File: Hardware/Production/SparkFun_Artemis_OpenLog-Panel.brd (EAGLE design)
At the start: 106.2 x 95.2 mm, 714 parts, among them J11 QWIIC_RIGHT_ANGLE, J14 CORTEX_JTAG, J16 CORTEX_JTAG, J17 MICRO-SD, J18 MICRO-SD, J19 QWIIC_RIGHT_ANGLE, J25 CORTEX_JTAG, J26 MICRO-SD, J27 QWIIC_RIGHT_ANGLE, J33 CORTEX_JTAG, J34 MICRO-SD, J35 QWIIC_RIGHT_ANGLE, J41 CORTEX_JTAG, J42 MICRO-SD, J43 QWIIC_RIGHT_ANGLE, J6 CORTEX_JTAG, J7 MICRO-SD, J8 QWIIC_RIGHT_ANGLE, Q1 20V/0.2A/8MHz/1.2Ω/1Vth, Q10 20V/0.2A/8MHz/1.2Ω/1Vth, Q11 20V/0.2A/8MHz/1.2Ω/1Vth, Q12 20V/4.2A/52mΩ/1.4W, Q13 20V/0.2A/8MHz/1.2Ω/1Vth, Q14 20V/0.2A/8MHz/1.2Ω/1Vth, Q15 20V/0.2A/8MHz/1.2Ω/1Vth, Q16 20V/0.2A/8MHz/1.2Ω/1Vth, Q17 20V/0.2A/8MHz/1.2Ω/1Vth, Q18 20V/4.2A/52mΩ/1.4W, Q19 20V/0.2A/8MHz/1.2Ω/1Vth, Q2 20V/0.2A/8MHz/1.2Ω/1Vth, Q20 20V/0.2A/8MHz/1.2Ω/1Vth, Q21 20V/0.2A/8MHz/1.2Ω/1Vth, Q22 20V/0.2A/8MHz/1.2Ω/1Vth, Q23 20V/0.2A/8MHz/1.2Ω/1Vth, Q24 20V/4.2A/52mΩ/1.4W, Q25 20V/0.2A/8MHz/1.2Ω/1Vth, Q26 20V/0.2A/8MHz/1.2Ω/1Vth, Q27 20V/0.2A/8MHz/1.2Ω/1Vth, Q28 20V/0.2A/8MHz/1.2Ω/1Vth, Q29 20V/0.2A/8MHz/1.2Ω/1Vth, Q3 20V/0.2A/8MHz/1.2Ω/1Vth, Q30 20V/4.2A/52mΩ/1.4W, Q31 20V/0.2A/8MHz/1.2Ω/1Vth, Q32 20V/0.2A/8MHz/1.2Ω/1Vth, Q33 20V/0.2A/8MHz/1.2Ω/1Vth, Q34 20V/0.2A/8MHz/1.2Ω/1Vth, Q35 20V/0.2A/8MHz/1.2Ω/1Vth, Q36 20V/4.2A/52mΩ/1.4W, Q4 20V/4.2A/52mΩ/1.4W, Q5 20V/0.2A/8MHz/1.2Ω/1Vth, Q6 20V/0.2A/8MHz/1.2Ω/1Vth, Q7 20V/0.2A/8MHz/1.2Ω/1Vth, Q8 20V/0.2A/8MHz/1.2Ω/1Vth, Q9 20V/0.2A/8MHz/1.2Ω/1Vth, U1 3.2V Supervisor, U10 CH340E, U11 AP2112K, U12 3.2V Supervisor, U13 ICM-20948, U14 1.8V/100mA, U15 MCP73831, U16 ARTEMIS_MODULESMD, U17 CH340E, U18 ICM-20948, U19 1.8V/100mA, U2 MCP73831, U20 AP2112K, U21 3.2V Supervisor, U22 MCP73831, U23 ARTEMIS_MODULESMD, U24 CH340E, U25 ICM-20948, U26 1.8V/100mA, U27 AP2112K, U28 3.2V Supervisor, U29 MCP73831, U3 AP2112K, U30 ARTEMIS_MODULESMD, U31 CH340E, U32 ICM-20948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

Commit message: PCB x03 commit for fab.
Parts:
- added C115, C116, C118, C119, C120: 0.1uF, SparkFun-Capacitors:0402-TIGHT
- added C117: 1.0nF, SparkFun-Capacitors:0402-TIGHT
- added C121, C122, C126: 1.0uF, SparkFun-Capacitors:0402-TIGHT
- added C123: 1.0uF, SparkFun-Capacitors:0603
- added C124: 2.2uF, SparkFun-Capacitors:0603
- added C125: 10uF, SparkFun-Capacitors:0603
- BT1, BT2, BT3, BT4, BT5, BT6: value ML414H_IV01E_BATTERY -> ML414H
- C10: value 10uF -> 15pF; device SparkFun-Capacitors:0603 -> SparkFun-Capacitors:0402-TIGHT
- C100, C105, C13, C39, C70, C91: value 0.1uF -> 1.0uF
- C101, C63: value 10uF -> 1.0uF; device SparkFun-Capacitors:0603 -> SparkFun-Capacitors:0402-TIGHT
- C102: device SparkFun-Capacitors:0402-TIGHT -> SparkFun-Capacitors:0603
- C103: value 10nF -> 2.2uF
- C104, C38, C62, C90: value 0.1uF -> 10uF; device SparkFun-Capacitors:0402-TIGHT -> SparkFun-Capacitors:0603
- C106, C28, C85, C86: value 0.1uF -> 4.7uF
- C107: value 1.0nF -> 4.7uF
- C108, C109, C66, C67, C87, C9: value 0.1uF -> 15pF
- C11, C20, C21, C55, C73, C74, C93: value 1.0uF -> 0.1uF
- C111, C83: value 1.0uF -> 10uF; device SparkFun-Capacitors:0402-TIGHT -> SparkFun-Capacitors:0603
- C113: value 1.0uF -> 10nF
- C114, C57, C76, C95: value 2.2uF -> 0.1uF; device SparkFun-Capacitors:0603 -> SparkFun-Capacitors:0402-TIGHT
- C12: value 10nF -> 10uF
- C14, C71: value 0.1uF -> 10nF; device SparkFun-Capacitors:0402-TIGHT -> SparkFun-Capacitors:0603
- C16: value 1.0nF -> 0.1uF
- C18: value 0.1uF -> 1.0nF
- C22: device SparkFun-Capacitors:0603 -> SparkFun-Capacitors:0402-TIGHT
- C23: value 2.2uF -> 1.0uF; device SparkFun-Capacitors:0603 -> SparkFun-Capacitors:0402-TIGHT
- C24: value 4.7uF -> 1.0uF; device SparkFun-Capacitors:0402-TIGHT -> SparkFun-Capacitors:0603
- C25: value 4.7uF -> 2.2uF; device SparkFun-Capacitors:0402-TIGHT -> SparkFun-Capacitors:0603
- C26: value 15pF -> 10uF; device SparkFun-Capacitors:0402 -> SparkFun-Capacitors:0603
- C27, C79, C80: value 15pF -> 1.0uF; device SparkFun-Capacitors:0402 -> SparkFun-Capacitors:0402-TIGHT
- C29, C30: device SparkFun-Capacitors:0402 -> SparkFun-Capacitors:0402-TIGHT
- C34: value 10uF -> 4.7uF; device SparkFun-Capacitors:0603 -> SparkFun-Capacitors:0402-TIGHT
- C35: value 1.0uF -> 15pF
- C36: value 10nF -> 15pF; device SparkFun-Capacitors:0603 -> SparkFun-Capacitors:0402-TIGHT
- C45: value 1.0nF -> 10nF; device SparkFun-Capacitors:0402-TIGHT -> SparkFun-Capacitors:0603
- C5: value 4.7uF -> 10uF; device SparkFun-Capacitors:0402-TIGHT -> SparkFun-Capacitors:0603
- C50: value 1.0uF -> 1.0nF
- C56, C94: value 1.0uF -> 0.1uF; device SparkFun-Capacitors:0603 -> SparkFun-Capacitors:0402-TIGHT
- C58, C59, C6: value 4.7uF -> 1.0uF
- C60: value 15pF -> 1.0uF; device SparkFun-Capacitors:0402 -> SparkFun-Capacitors:0603
- C61: value 15pF -> 2.2uF; device SparkFun-Capacitors:0402 -> SparkFun-Capacitors:0603
- C64: value 1.0uF -> 4.7uF
- C65: value 10nF -> 4.7uF; device SparkFun-Capacitors:0603 -> SparkFun-Capacitors:0402-TIGHT
- C69: value 1.0nF -> 10uF; device SparkFun-Capacitors:0402-TIGHT -> SparkFun-Capacitors:0603
- C7, C8: value 15pF -> 4.7uF; device SparkFun-Capacitors:0402 -> SparkFun-Capacitors:0402-TIGHT
- C75: value 1.0uF -> 1.0nF; device SparkFun-Capacitors:0603 -> SparkFun-Capacitors:0402-TIGHT
- C77, C78, C97: value 4.7uF -> 0.1uF
- C81: value 0.1uF -> 1.0uF; device SparkFun-Capacitors:0402-TIGHT -> SparkFun-Capacitors:0603
- C82: value 10uF -> 2.2uF
- C84: value 10nF -> 1.0uF; device SparkFun-Capacitors:0603 -> SparkFun-Capacitors:0402-TIGHT
- C88: value 1.0nF -> 15pF
- C92: value 1.0uF -> 10nF; device SparkFun-Capacitors:0402-TIGHT -> SparkFun-Capacitors:0603
- C96: value 4.7uF -> 1.0nF
- C98, C99: value 15pF -> 0.1uF; device SparkFun-Capacitors:0402 -> SparkFun-Capacitors:0402-TIGHT
- D14, D21, D28, D35, D42: value 3A/10V/280mV -> 1A/23V/620mV
- D4: value 3A/10V/280mV -> Yellow; device SparkFun-DiscreteSemi:SOD-323 -> SparkFun-LED:LED-0603
- D5: value Yellow -> BLUE
- D6: value BLUE -> 1A/23V/620mV; device SparkFun-LED:LED-0603 -> SparkFun-DiscreteSemi:SOD-323
- J11, J19, J27, J35, J43, J8: value QWIIC_RIGHT_ANGLE -> (none)
- moved C59 91.2 mm to (91.2, 8.64)
- moved C62 84.4 mm to (89.9, 7.11)
- moved C63 82.6 mm to (89.9, 5.97), turned to 0 degrees
- moved C58 79.0 mm to (86.1, 17.8), turned to 270 degrees
- moved C61 69.8 mm to (75.9, 10.2), flipped to the bottom
- moved C60 69.3 mm to (67.1, 6.35), flipped to the bottom, turned to 270 degrees
- moved C81 46.3 mm to (5.08, 41.9), flipped to the bottom, turned to 270 degrees
- moved C102 46.1 mm to (36.1, 41.9), flipped to the bottom, turned to 270 degrees
- moved C82 37.9 mm to (14.0, 45.7), flipped to the bottom, turned to 90 degrees
- moved C103 37.8 mm to (45.0, 45.7), turned to 90 degrees
- moved C24 36.2 mm to (36.1, 6.35), turned to 270 degrees
- moved C97 31.0 mm to (39.9, 54.6), flipped to the top
- moved D6 29.6 mm to (23.9, 18.7), turned to 0 degrees
- moved C56 27.2 mm to (88.6, 22.9), turned to 90 degrees
- moved C99 26.6 mm to (55.1, 44.5), flipped to the bottom, turned to 270 degrees
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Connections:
- net 3.3V: now also C5.1, C6.1, D6.A, Q4.2; no longer D4.A, Q4.3, R1.2, R28.2
- net 3.3V1: now also C14.1, C15.1, C25.1, C26.1, C27.1, Q12.2; no longer C12.1, C13.1, C21.1, Q12.3, R13.2, R31.2
- net 3.3V2: now also C45.1, C47.1, C59.1, C61.1, C62.1, C63.1, Q18.2; no longer C36.1, C37.1, C55.1, C57.1, Q18.3, R43.2, R59.2
- net 3.3V3: now also C71.1, C72.1, C80.1, C82.1, C83.1, C84.1, Q24.2; no longer C65.1, C66.1, C74.1, C76.1, Q24.3, R69.2, R79.2
- net 3.3V4: now also C101.1, C103.1, C104.1, C105.1, C92.1, Q30.2; no longer C84.1, C85.1, C95.1, Q30.3, R89.2, R99.2
- net 3.3V5: now also C113.1, C122.1, C124.1, C125.1, C126.1, Q36.2; no longer C103.1, C104.1, C112.1, Q36.3, R109.2, R119.2
- net 5V1: now also C8.1, D4.A; no longer C6.1, D5.A
- net 5V2: now also C34.1; no longer C25.1
- net 5V3: now also C65.1; no longer C59.1
- net 5V4: now also C86.1; no longer C78.1
- net 5V5: now also C107.1; no longer C97.1
- net ARTEMIS_!RESET1: now also C16.2, C18.1; no longer C14.2, C16.1
- net ARTEMIS_!RESET2: now also C48.2, C50.1; no longer C38.2, C45.1
- net ARTEMIS_!RESET3: now also C73.2, C75.1; no longer C67.2, C69.1
- net ARTEMIS_!RESET4: now also C94.2, C96.1; no longer C86.2, C88.1
- net ARTEMIS_!RESET5: now also C115.2, C117.1; no longer C105.2, C107.1
- net ARTEMIS_!RTS!1: now also C16.1, C17.1; no longer C14.1, C15.1
- net ARTEMIS_!RTS!2: now also C48.1, C49.1; no longer C38.1, C39.1
- net ARTEMIS_!RTS!3: now also C73.1, C74.1; no longer C67.1, C68.1
- net ARTEMIS_!RTS!4: now also C94.1, C95.1; no longer C86.1, C87.1
- net ARTEMIS_!RTS!5: now also C115.1, C116.1; no longer C105.1, C106.1
- net ARTEMIS_BOOT1: now also C17.2; no longer C15.2
- net ARTEMIS_BOOT2: now also C49.2; no longer C39.2
- net ARTEMIS_BOOT3: now also C74.2; no longer C68.2
- net ARTEMIS_BOOT4: now also C95.2; no longer C87.2
- net ARTEMIS_BOOT5: now also C116.2; no longer C106.2
- net GND: now also C5.2, C6.2
- net GND1: now also C10.1, C11.1, C14.2, C15.2, C24.2, C25.2, C26.2, C27.2, C7.2, C8.2, D5.C; no longer C10.2, C11.2, C16.2, C17.2, C5.2, C6.2, C7.1, C8.1, D6.C
- net GND2: now also C28.2, C35.1, C36.1, C37.1, C38.2, C39.2, C58.2, C59.2, C60.2, C61.2, C62.2, C63.2; no longer C24.2, C25.2, C26.1, C27.1, C28.1, C35.2, C36.2, C37.2, C48.2, C49.2
- net GND3: now also C66.1, C67.1, C68.1, C77.2, C78.2, C79.2, C80.2, C81.2, C82.2, C83.2, C84.2; no longer C58.2, C59.2, C60.1, C61.1, C62.1, C63.2, C66.2, C73.2, C74.2
- net GND4: now also C100.2, C101.2, C102.2, C103.2, C104.2, C105.2, C86.2, C87.1, C88.1, C89.1, C96.2, C97.2, C98.2, C99.2; no longer C77.2, C78.2, C79.1, C80.1, C81.1, C82.2, C83.2, C84.2, C88.2, C89.2, C94.2, C95.2
- net GND5: now also C106.2, C108.1, C109.1, C110.1, C117.2, C118.2, C119.2, C120.2, C121.2, C122.2, C123.2, C124.2, C125.2, C126.2; no longer C100.1, C101.2, C102.2, C103.2, C104.2, C108.2, C109.2, C110.2, C96.2, C97.2, C98.1, C99.1
- net ICM-20948-LV_#_1.8V1: now also C21.1, C22.1; no longer C19.1, C20.1
- net ICM-20948-LV_#_1.8V2: now also C57.1, C58.1; no longer C49.1, C50.1
- net ICM-20948-LV_#_1.8V3: now also C78.1, C79.1; no longer C72.1, C73.1
- net ICM-20948-LV_#_1.8V4: now also C100.1, C99.1; no longer C91.1, C92.1
- net ICM-20948-LV_#_1.8V5: now also C120.1, C121.1; no longer C110.1, C111.1
- net MICROSD_PWR1: now also C19.1; no longer C17.1
- net MICROSD_PWR2: now also C55.1; no longer C47.1
- net MICROSD_PWR3: now also C76.1; no longer C70.1
- net MICROSD_PWR4: now also C97.1; no longer C89.1
- net MICROSD_PWR5: now also C118.1; no longer C108.1
- net N$10: now also D5.A; no longer D6.A
- net N$14: now also C20.1; no longer C18.1
- net N$17: now also Q12.3; no longer Q12.2
- net N$22: now also C35.2; no longer C26.2
- net N$23: now also C36.2; no longer C27.2
- net N$3: now also D4.C; no longer D5.C
- net N$33: now also C56.1; no longer C48.1
- net N$36: now also Q18.3; no longer Q18.2
- net N$39: now also C66.2; no longer C60.2
- net N$40: now also C67.2; no longer C61.2
- net N$45: now also C77.1; no longer C71.1
- net N$48: now also Q24.3; no longer Q24.2
- net N$5: now also Q4.3; no longer Q4.2
- net N$51: now also C87.2; no longer C79.2
- net N$52: now also C88.2; no longer C80.2
- net N$57: now also C98.1; no longer C90.1
- net N$6: now also C9.2; no longer C7.2
- net N$60: now also Q30.3; no longer Q30.2
- net N$63: now also C108.2; no longer C98.2
- net N$64: now also C109.2; no longer C99.2
- net N$69: now also C119.1; no longer C109.1
- net N$72: now also Q36.3; no longer Q36.2
- net N$8: now also C10.2; no longer C8.2
- net VCC_1: now also D6.C, R1.2, R28.2; no longer D4.C
- net VCC_2: now also C11.2, C12.1, C13.1, R13.2, R31.2; no longer C10.1, C11.1, C9.2
- net VCC_3: now also C37.2, C38.1, C39.1, R43.2, R59.2; no longer C28.2, C34.1, C35.1
- net VCC_4: now also C68.2, C69.1, C70.1, R69.2, R79.2; no longer C62.2, C63.1, C64.1
- net VCC_5: now also C89.2, C90.1, C91.1, R89.2, R99.2; no longer C81.2, C82.1, C83.1
- net VCC_6: now also C110.2, C111.1, C112.1, R109.2, R119.2; no longer C100.2, C101.1, C102.1
- net VIN1: now also C24.1; no longer C22.1
- net VIN2: now also C60.1; no longer C56.1
- net VIN3: now also C81.1; no longer C75.1
- net VIN4: now also C102.1; no longer C94.1
- net VIN5: now also C123.1; no longer C113.1
- net V_BATT1: now also C7.1; no longer C5.1
- net V_BATT2: now also C28.1; no longer C24.1
- net V_BATT3: now also C64.1; no longer C58.1
- net V_BATT4: now also C85.1; no longer C77.1
- net V_BATT5: now also C106.1; no longer C96.1
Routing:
- net VCC_6: track 10.2 -> 26.6 mm, vias 0 -> 1
- net VCC_5: track 10.2 -> 26.6 mm, vias 0 -> 1
- net VCC_2: track 10.2 -> 26.6 mm, vias 0 -> 1
- net VCC_4: track 10.2 -> 26.6 mm, vias 0 -> 1
- net VCC_3: track 10.2 -> 26.6 mm, vias 0 -> 1
- net VCC_1: track 10.2 -> 26.6 mm, vias 0 -> 1
- net N$5: track 5.89 -> 9.18 mm
- net N$48: track 5.89 -> 9.18 mm
- net N$72: track 5.89 -> 9.18 mm
- net N$60: track 5.89 -> 9.18 mm
- net N$36: track 5.89 -> 9.18 mm
- net N$17: track 5.89 -> 9.18 mm
- net GND3: track 6.76 -> 5.17 mm
- net GND5: track 6.76 -> 5.17 mm
- net GND4: track 6.76 -> 5.17 mm
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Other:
- board text added: "x03"
- board text removed: "x02"

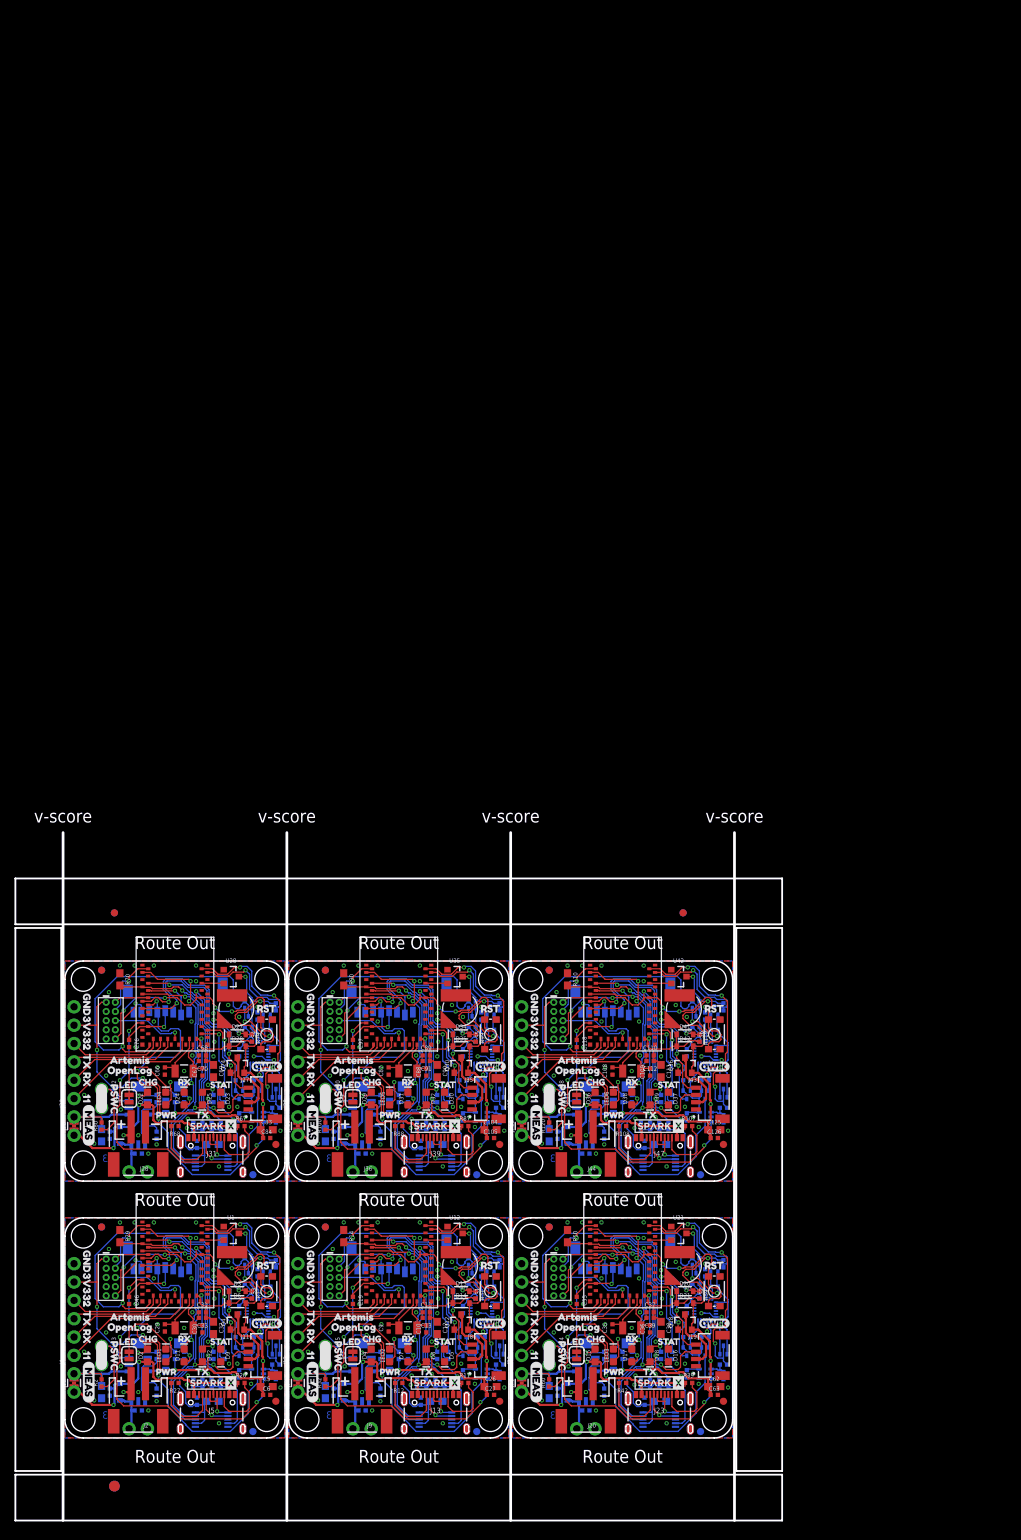
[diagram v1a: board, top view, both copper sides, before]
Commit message: Add BME280 and CCS811 support. Refactor TimeStamp menu.
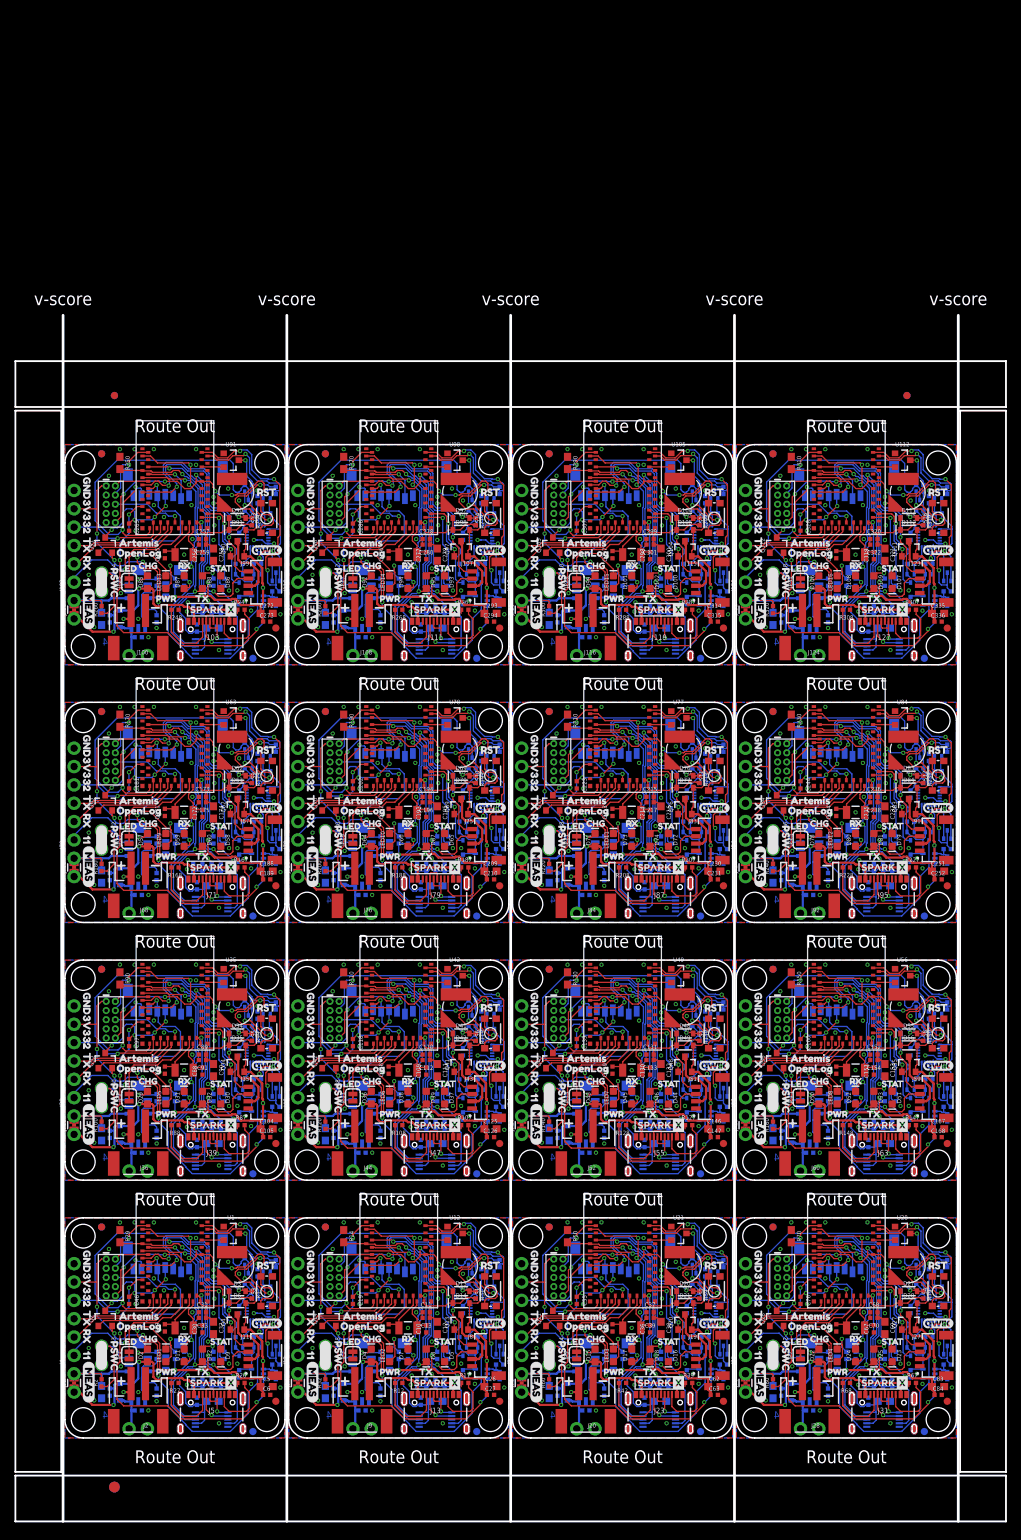
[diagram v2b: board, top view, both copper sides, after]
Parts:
- added BT10, BT11, BT12, BT13, BT14, BT15, BT16, BT7, BT8, BT9: ML414H, SparkFun-Batteries:ML414H_IV01E
- added C127, C128, C148, C149, C169, C170, C190, C191, C211, C212, C232, C233, C253, C254, C274, C275, C295, C296, C316, C317: 4.7uF, SparkFun-Capacitors:0402-TIGHT
- added C129, C130, C150, C151, C171, C172, C192, C193, C213, C214, C234, C235, C255, C256, C276, C277, C297, C298, C318, C319: 15pF, SparkFun-Capacitors:0402-TIGHT
- added C131, C135, C136, C137, C139, C140, C141, C152, C156, C157, C158, C160, C161, C162, C173, C177, C178, C179, C181, C182, C183, C194, C198, C199, C200, C202, C203, C204, C215, C219, C220, C221, C223, C224, C225, C236, C240, C241, C242, C244, C245, C246, C257, C261, C262, C263, C265, C266, C267, C278, C282, C283, C284, C286, C287, C288, C299, C303, C304, C305, C307, C308, C309, C320, C324, C325, C326, C328, C329, C330: 0.1uF, SparkFun-Capacitors:0402-TIGHT
- added C132, C146, C153, C167, C174, C188, C195, C209, C216, C230, C237, C251, C258, C272, C279, C293, C300, C314, C321, C335: 10uF, SparkFun-Capacitors:0603
- added C133, C142, C143, C147, C154, C163, C164, C168, C175, C184, C185, C189, C196, C205, C206, C210, C217, C226, C227, C231, C238, C247, C248, C252, C259, C268, C269, C273, C280, C289, C290, C294, C301, C310, C311, C315, C322, C331, C332, C336: 1.0uF, SparkFun-Capacitors:0402-TIGHT
- added C134, C155, C176, C197, C218, C239, C260, C281, C302, C323: 10nF, SparkFun-Capacitors:0603
- added C138, C159, C180, C201, C222, C243, C264, C285, C306, C327: 1.0nF, SparkFun-Capacitors:0402-TIGHT
- added C144, C165, C186, C207, C228, C249, C270, C291, C312, C333: 1.0uF, SparkFun-Capacitors:0603
- added C145, C166, C187, C208, C229, C250, C271, C292, C313, C334: 2.2uF, SparkFun-Capacitors:0603
- added D100, D107, D44, D51, D58, D65, D72, D79, D86, D93: BLUE, SparkFun-LED:LED-0603
- added D101, D106, D108, D43, D45, D50, D52, D57, D59, D64, D66, D71, D73, D78, D80, D85, D87, D92, D94, D99: Yellow, SparkFun-LED:LED-0603
- added D102, D109, D46, D53, D60, D67, D74, D81, D88, D95: GREEN, SparkFun-LED:LED-0603
- added D103, D104, D110, D111, D47, D48, D54, D55, D61, D62, D68, D69, D75, D76, D82, D83, D89, D90, D96, D97: 3A/10V/280mV, SparkFun-DiscreteSemi:SOD-323
- added D105, D112, D49, D56, D63, D70, D77, D84, D91, D98: 1A/23V/620mV, SparkFun-DiscreteSemi:SOD-323
- added FD25, FD26, FD27, FD28, FD29, FD30, FD31, FD32, FD33, FD34, FD35, FD36, FD37, FD38, FD39, FD40, FD41, FD42, FD43, FD44, FD45, FD46, FD47, FD48, FD49, FD50, FD51, FD52, FD53, FD54, FD55, FD56, FD57, FD58, FD59, FD60, FD61, FD62, FD63, FD64: FIDUCIAL1X2, SparkFun-Aesthetics:FIDUCIAL-1X2
- added H25, H26, H27, H28, H29, H30, H31, H32, H33, H34, H35, H36, H37, H38, H39, H40, H41, H42, H43, H44, H45, H46, H47, H48, H49, H50, H51, H52, H53, H54, H55, H56, H57, H58, H59, H60, H61, H62, H63, H64: STAND-OFF, SparkFun-Hardware:STAND-OFF
- added J100, J108, J116, J124, J52, J60, J68, J76, J84, J92: (no value), SparkFun-Connectors:JST-2-SMD
- added J101, J104, J109, J112, J117, J120, J125, J128, J53, J56, J61, J64, J69, J72, J77, J80, J85, J88, J93, J96: (no value), SparkFun-Connectors:1X02_NO_SILK
- added J102, J110, J118, J126, J54, J62, J70, J78, J86, J94: (no value), SparkFun-Connectors:1X06_NO_SILK
- added J103, J111, J119, J127, J55, J63, J71, J79, J87, J95: (no value), USBC:USB-C-16P-5
- added J105, J113, J121, J49, J57, J65, J73, J81, J89, J97: CORTEX_JTAG, SparkFun-Connectors:2X5-PTH-1.27MM
- added J106, J114, J122, J50, J58, J66, J74, J82, J90, J98: MICRO-SD, SparkFun-Connectors:MICRO-SD-SOCKET
- added J107, J115, J123, J51, J59, J67, J75, J83, J91, J99: (no value), SparkFun-Connectors:JST04_1MM_RA
- added JP13, JP15, JP17, JP19, JP21, JP23, JP25, JP27, JP29, JP31: (no value), SparkFun-Jumpers:SMT-JUMPER_2_NC_TRACE_SILK
- added JP14, JP16, JP18, JP20, JP22, JP24, JP26, JP28, JP30, JP32: MEAS, SparkFun-Jumpers:COMBO-JUMPER_2_NC_TRACE
- added LED10, LED11, LED12, LED13, LED14, LED15, LED16, LED7, LED8, LED9: RED, SparkFun-LED:LED-0603
- added LOGO10, LOGO11, LOGO12, LOGO13, LOGO14, LOGO15, LOGO16, LOGO7, LOGO8, LOGO9: OSHW-LOGOS, SparkFun-Aesthetics:OSHW-LOGO-S
- added Q100, Q101, Q102, Q103, Q106, Q107, Q108, Q109, Q110, Q37, Q38, Q39, Q40, Q43, Q44, Q45, Q46, Q47, Q50, Q51, Q52, Q53, Q54, Q57, Q58, Q59, Q60, Q61, Q64, Q65, Q66, Q67, Q68, Q71, Q72, Q73, Q74, Q75, Q78, Q79, Q80, Q81, Q82, Q85, Q86, Q87, Q88, Q89, Q92, Q93, Q94, Q95, Q96, Q99: 20V/0.2A/8MHz/1.2Ω/1Vth, SparkFun-DiscreteSemi:SOT-416FL
- added Q104, Q105, Q111, Q112, Q41, Q42, Q48, Q49, Q55, Q56, Q62, Q63, Q69, Q70, Q76, Q77, Q83, Q84, Q90, Q91, Q97, Q98: 20V/4.2A/52mΩ/1.4W, SparkFun-DiscreteSemi:SOT23-3
- added R121, R131, R132, R133, R134, R135, R136, R137, R138, R141, R151, R152, R153, R154, R155, R156, R157, R158, R161, R171, R172, R173, R174, R175, R176, R177, R178, R181, R191, R192, R193, R194, R195, R196, R197, R198, R201, R211, R212, R213, R214, R215, R216, R217, R218, R221, R231, R232, R233, R234, R235, R236, R237, R238, R241, R251, R252, R253, R254, R255, R256, R257, R258, R261, R271, R272, R273, R274, R275, R276, R277, R278, R281, R291, R292, R293, R294, R295, R296, R297, R298, R301, R311, R312, R313, R314, R315, R316, R317, R318: 2.2k, SparkFun-Resistors:0402-TIGHT
- added R122, R123, R124, R125, R126, R139, R142, R143, R144, R145, R146, R159, R162, R163, R164, R165, R166, R179, R182, R183, R184, R185, R186, R199, R202, R203, R204, R205, R206, R219, R222, R223, R224, R225, R226, R239, R242, R243, R244, R245, R246, R259, R262, R263, R264, R265, R266, R279, R282, R283, R284, R285, R286, R299, R302, R303, R304, R305, R306, R319: 1k, SparkFun-Resistors:0402-TIGHT
- added R127, R128, R147, R148, R167, R168, R187, R188, R207, R208, R227, R228, R247, R248, R267, R268, R287, R288, R307, R308: 5.1k, SparkFun-Resistors:0402-TIGHT
- added R129, R149, R169, R189, R209, R229, R249, R269, R289, R309: 100k, SparkFun-Resistors:0402-TIGHT
- added R130, R150, R170, R190, R210, R230, R250, R270, R290, R310: 220k, SparkFun-Resistors:0603
- added R140, R160, R180, R200, R220, R240, R260, R280, R300, R320: 10k, SparkFun-Resistors:0402-TIGHT
- added S10, S11, S12, S13, S14, S15, S16, S7, S8, S9: RESET, SparkFun-Switches:TACTILE_SWITCH_SMD_4.6X2.8MM
- added U$217, U$253, U$289, U$325, U$361, U$397, U$433, U$469, U$505, U$541: (no value), buzzard_labels (2):MEAS3
- added U$218, U$224, U$254, U$260, U$290, U$296, U$326, U$332, U$362, U$368, U$398, U$404, U$434, U$440, U$470, U$476, U$506, U$512, U$542, U$548: (no value), buzzard_labels (1):X0
- added U$219, U$225, U$255, U$261, U$291, U$297, U$327, U$333, U$363, U$369, U$399, U$405, U$435, U$441, U$471, U$477, U$507, U$513, U$543, U$549: (no value), buzzard_labels (1):Y1
- added U$220, U$226, U$256, U$262, U$292, U$298, U$328, U$334, U$364, U$370, U$400, U$406, U$436, U$442, U$472, U$478, U$508, U$514, U$544, U$550: (no value), buzzard_labels (1):Z2
- added U$221, U$257, U$293, U$329, U$365, U$401, U$437, U$473, U$509, U$545: (no value), buzzard_labels (1):G5
- added U$222, U$258, U$294, U$330, U$366, U$402, U$438, U$474, U$510, U$546: (no value), buzzard_labels (1):A4
- added U$223, U$259, U$295, U$331, U$367, U$403, U$439, U$475, U$511, U$547: (no value), buzzard_labels (1):M3
- added U$227, U$263, U$299, U$335, U$371, U$407, U$443, U$479, U$515, U$551: (no value), qwiic#logo#jpg:QWIIC#LOGO#JPG
- added U$228, U$264, U$300, U$336, U$372, U$408, U$444, U$480, U$516, U$552: (no value), buzzard_labels (12):CHG2
- added U$229, U$265, U$301, U$337, U$373, U$409, U$445, U$481, U$517, U$553: (no value), buzzard_labels (12):PWR0
- added U$230, U$266, U$302, U$338, U$374, U$410, U$446, U$482, U$518, U$554: (no value), buzzard_labels (12):RX4
- added U$231, U$267, U$303, U$339, U$375, U$411, U$447, U$483, U$519, U$555: (no value), buzzard_labels (12):STAT5
- added U$232, U$268, U$304, U$340, U$376, U$412, U$448, U$484, U$520, U$556: (no value), buzzard_labels (12):TX3
- added U$233, U$269, U$305, U$341, U$377, U$413, U$449, U$485, U$521, U$557: (no value), buzzard_labels (13):ARTEMIS13
- added U$234, U$270, U$306, U$342, U$378, U$414, U$450, U$486, U$522, U$558: (no value), buzzard_labels (13):OPENLOG12
- added U$235, U$271, U$307, U$343, U$379, U$415, U$451, U$487, U$523, U$559: (no value), buzzard_labels (13):RST9
- added U$236, U$272, U$308, U$344, U$380, U$416, U$452, U$488, U$524, U$560: (no value), buzzard_labels (13):VIN8
- added U$237, U$238, U$273, U$274, U$309, U$310, U$345, U$346, U$381, U$382, U$417, U$418, U$453, U$454, U$489, U$490, U$525, U$526, U$561, U$562: (no value), buzzard_labels (14):3V34
- added U$239, U$240, U$275, U$276, U$311, U$312, U$347, U$348, U$383, U$384, U$419, U$420, U$455, U$456, U$491, U$492, U$527, U$528, U$563, U$564: (no value), buzzard_labels (14):113
- added U$241, U$242, U$277, U$278, U$313, U$314, U$349, U$350, U$385, U$386, U$421, U$422, U$457, U$458, U$493, U$494, U$529, U$530, U$565, U$566: (no value), buzzard_labels (14):322
- added U$243, U$244, U$279, U$280, U$315, U$316, U$351, U$352, U$387, U$388, U$423, U$424, U$459, U$460, U$495, U$496, U$531, U$532, U$567, U$568: (no value), buzzard_labels (14):GND5
- added U$245, U$246, U$281, U$282, U$317, U$318, U$353, U$354, U$389, U$390, U$425, U$426, U$461, U$462, U$497, U$498, U$533, U$534, U$569, U$570: (no value), buzzard_labels (14):RX1
- added U$247, U$248, U$283, U$284, U$319, U$320, U$355, U$356, U$391, U$392, U$427, U$428, U$463, U$464, U$499, U$500, U$535, U$536, U$571, U$572: (no value), buzzard_labels (14):TX0
- added U$249, U$285, U$321, U$357, U$393, U$429, U$465, U$501, U$537, U$573: SPARKX-LOGO3, SparkX:SPARKX-SMALL
- added U$250, U$286, U$322, U$358, U$394, U$430, U$466, U$502, U$538, U$574: (no value), buzzard_labels (15):LED0
- added U$251, U$252, U$287, U$288, U$323, U$324, U$359, U$360, U$395, U$396, U$431, U$432, U$467, U$468, U$503, U$504, U$539, U$540, U$575, U$576: (no value), buzzard_labels:PSWC0
- added U100, U107, U44, U51, U58, U65, U72, U79, U86, U93: ARTEMIS_MODULESMD, SparkFun-IC-Microcontroller:ARTEMIS_FP
- added U101, U108, U45, U52, U59, U66, U73, U80, U87, U94: CH340E, SparkFun-IC-Comms:MSOP10
- added U102, U109, U46, U53, U60, U67, U74, U81, U88, U95: ICM-20948, SparkFun-Sensors:QFN24-3X3
- added U103, U110, U47, U54, U61, U68, U75, U82, U89, U96: 1.8V/100mA, SparkFun-IC-Power:SC70
- added U104, U111, U48, U55, U62, U69, U76, U83, U90, U97: AP2112K, SparkFun-IC-Power:SOT23-5
- added U105, U112, U49, U56, U63, U70, U77, U84, U91, U98: 3.0V Supervisor, SparkFun-IC-Power:SOT23-3
- added U106, U43, U50, U57, U64, U71, U78, U85, U92, U99: MCP73831, SparkFun-IC-Power:SOT23-5
- added Y10, Y11, Y12, Y13, Y14, Y15, Y16, Y7, Y8, Y9: 32.768kHz, SparkFun-Clocks:CRYSTAL-SMD-3.2X1.5MM
- Q12, Q18, Q24, Q30, Q36: value 20V/4.2A/52mΩ/1.4W -> 20V/0.2A/8MHz/1.2Ω/1Vth; device SparkFun-DiscreteSemi:SOT23-3 -> SparkFun-DiscreteSemi:SOT-416FL
- Q13, Q14, Q2, Q20, Q21, Q27, Q28, Q34, Q35: value 20V/0.2A/8MHz/1.2Ω/1Vth -> 20V/4.2A/52mΩ/1.4W; device SparkFun-DiscreteSemi:SOT-416FL -> SparkFun-DiscreteSemi:SOT23-3
- U1, U12, U21, U28, U35, U42: value 3.2V Supervisor -> 3.0V Supervisor
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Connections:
- new net !POWER_LOSS!10: U72.D3, U77.2
- new net !POWER_LOSS!11: U79.D3, U84.2
- new net !POWER_LOSS!12: U86.D3, U91.2
- new net !POWER_LOSS!13: U93.D3, U98.2
- new net !POWER_LOSS!14: U100.D3, U105.2
- new net !POWER_LOSS!15: U107.D3, U112.2
- new net !POWER_LOSS!6: U44.D3, U49.2
- new net !POWER_LOSS!7: U51.D3, U56.2
- new net !POWER_LOSS!8: U58.D3, U63.2
- new net !POWER_LOSS!9: U65.D3, U70.2
- new net 3.3V10: C218.1, C219.1, C227.1, C229.1, C230.1, C231.1, D77.A, J81.1, J86.5, Q76.2, Q77.2, R203.2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
- new net 3.3V11: C239.1, C240.1, C248.1, C250.1, C251.1, C252.1, D84.A, J89.1, J94.5, Q83.2, Q84.2, R223.2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
- new net 3.3V12: C260.1, C261.1, C269.1, C271.1, C272.1, C273.1, D91.A, J102.5, J97.1, Q90.2, Q91.2, R243.2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
- new net 3.3V13: C281.1, C282.1, C290.1, C292.1, C293.1, C294.1, D98.A, J105.1, J110.5, Q97.2, Q98.2, R263.2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
- new net 3.3V14: C302.1, C303.1, C311.1, C313.1, C314.1, C315.1, D105.A, J113.1, J118.5, Q104.2, Q105.2, R283.2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
- new net 3.3V15: C323.1, C324.1, C332.1, C334.1, C335.1, C336.1, D112.A, J121.1, J126.5, Q111.2, Q112.2, R303.2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
- new net 3.3V6: C134.1, C135.1, C143.1, C145.1, C146.1, C147.1, D49.A, J49.1, J54.5, Q48.2, Q49.2, R123.2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
- new net 3.3V7: C155.1, C156.1, C164.1, C166.1, C167.1, C168.1, D56.A, J57.1, J62.5, Q55.2, Q56.2, R143.2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
- new net 3.3V8: C176.1, C177.1, C185.1, C187.1, C188.1, C189.1, D63.A, J65.1, J70.5, Q62.2, Q63.2, R163.2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
- new net 3.3V9: C197.1, C198.1, C206.1, C208.1, C209.1, C210.1, D70.A, J73.1, J78.5, Q69.2, Q70.2, R183.2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
- new net 5V10: C212.1, D71.A, D75.C, J87.VBUS1, J87.VBUS2, JP22.1, JP22.3, U71.4
- new net 5V11: C233.1, D78.A, D82.C, J95.VBUS1, J95.VBUS2, JP24.1, JP24.3, U78.4
- new net 5V12: C254.1, D85.A, D89.C, J103.VBUS1, J103.VBUS2, JP26.1, JP26.3, U85.4
- new net 5V13: C275.1, D92.A, D96.C, J111.VBUS1, J111.VBUS2, JP28.1, JP28.3, U92.4
- new net 5V14: C296.1, D103.C, D99.A, J119.VBUS1, J119.VBUS2, JP30.1, JP30.3, U99.4
- new net 5V15: C317.1, D106.A, D110.C, J127.VBUS1, J127.VBUS2, JP32.1, JP32.3, U106.4
- new net 5V6: C128.1, D43.A, D47.C, J55.VBUS1, J55.VBUS2, JP14.1, JP14.3, U43.4
- new net 5V7: C149.1, D50.A, D54.C, J63.VBUS1, J63.VBUS2, JP16.1, JP16.3, U50.4
- new net 5V8: C170.1, D57.A, D61.C, J71.VBUS1, J71.VBUS2, JP18.1, JP18.3, U57.4
- new net 5V9: C191.1, D64.A, D68.C, J79.VBUS1, J79.VBUS2, JP20.1, JP20.3, U64.4
- new net ARTEMIS_!RESET10: C220.2, C222.1, J81.10, R209.1, S11.3, S11.4, U72.~RST
- new net ARTEMIS_!RESET11: C241.2, C243.1, J89.10, R229.1, S12.3, S12.4, U79.~RST
- new net ARTEMIS_!RESET12: C262.2, C264.1, J97.10, R249.1, S13.3, S13.4, U86.~RST
- new net ARTEMIS_!RESET13: C283.2, C285.1, J105.10, R269.1, S14.3, S14.4, U93.~RST
- new net ARTEMIS_!RESET14: C304.2, C306.1, J113.10, R289.1, S15.3, S15.4, U100.~RST
- new net ARTEMIS_!RESET15: C325.2, C327.1, J121.10, R309.1, S16.3, S16.4, U107.~RST
- new net ARTEMIS_!RESET6: C136.2, C138.1, J49.10, R129.1, S7.3, S7.4, U44.~RST
- new net ARTEMIS_!RESET7: C157.2, C159.1, J57.10, R149.1, S8.3, S8.4, U51.~RST
- new net ARTEMIS_!RESET8: C178.2, C180.1, J65.10, R169.1, S9.3, S9.4, U58.~RST
- new net ARTEMIS_!RESET9: C199.2, C201.1, J73.10, R189.1, S10.3, S10.4, U65.~RST
- new net ARTEMIS_!RTS!10: C220.1, C221.1, U73.4
- new net ARTEMIS_!RTS!11: C241.1, C242.1, U80.4
- new net ARTEMIS_!RTS!12: C262.1, C263.1, U87.4
- new net ARTEMIS_!RTS!13: C283.1, C284.1, U94.4
- new net ARTEMIS_!RTS!14: C304.1, C305.1, U101.4
- new net ARTEMIS_!RTS!15: C325.1, C326.1, U108.4
- new net ARTEMIS_!RTS!6: C136.1, C137.1, U45.4
- new net ARTEMIS_!RTS!7: C157.1, C158.1, U52.4
- new net ARTEMIS_!RTS!8: C178.1, C179.1, U59.4
- new net ARTEMIS_!RTS!9: C199.1, C200.1, U66.4
- new net ARTEMIS_BOOT10: C221.2, R210.2, U72.BOOT
- new net ARTEMIS_BOOT11: C242.2, R230.2, U79.BOOT
- new net ARTEMIS_BOOT12: C263.2, R250.2, U86.BOOT
- new net ARTEMIS_BOOT13: C284.2, R270.2, U93.BOOT
- new net ARTEMIS_BOOT14: C305.2, R290.2, U100.BOOT
- new net ARTEMIS_BOOT15: C326.2, R310.2, U107.BOOT
- new net ARTEMIS_BOOT6: C137.2, R130.2, U44.BOOT
- new net ARTEMIS_BOOT7: C158.2, R150.2, U51.BOOT
- new net ARTEMIS_BOOT8: C179.2, R170.2, U58.BOOT
- new net ARTEMIS_BOOT9: C200.2, R190.2, U65.BOOT
- new net ARTEMIS_D37: J49.6, U44.~AD33/SWO
- new net ARTEMIS_D38: U44.~AD29
- new net ARTEMIS_D39: U44.~AD35
- new net ARTEMIS_D40: U44.~AD31
- new net ARTEMIS_D41: U44.AD16
- new net ARTEMIS_D42: U44.AD34
- new net ARTEMIS_D43: J57.6, U51.~AD33/SWO
- new net ARTEMIS_D44: U51.~AD29
- new net ARTEMIS_D45: U51.~AD35
- new net ARTEMIS_D46: U51.~AD31
- new net ARTEMIS_D47: U51.AD16
- new net ARTEMIS_D48: U51.AD34
- new net ARTEMIS_D49: J65.6, U58.~AD33/SWO
- new net ARTEMIS_D50: U58.~AD29
- new net ARTEMIS_D51: U58.~AD35
- new net ARTEMIS_D52: U58.~AD31
- new net ARTEMIS_D53: U58.AD16
- new net ARTEMIS_D54: U58.AD34
- new net ARTEMIS_D55: J73.6, U65.~AD33/SWO
- new net ARTEMIS_D56: U65.~AD29
- new net ARTEMIS_D57: U65.~AD35
- new net ARTEMIS_D58: U65.~AD31
- new net ARTEMIS_D59: U65.AD16
- new net ARTEMIS_D60: U65.AD34
- new net ARTEMIS_D61: J81.6, U72.~AD33/SWO
- new net ARTEMIS_D62: U72.~AD29
- new net ARTEMIS_D63: U72.~AD35
- new net ARTEMIS_D64: U72.~AD31
- new net ARTEMIS_D65: U72.AD16
- new net ARTEMIS_D66: U72.AD34
- new net ARTEMIS_D67: J89.6, U79.~AD33/SWO
- new net ARTEMIS_D68: U79.~AD29
- new net ARTEMIS_D69: U79.~AD35
- new net ARTEMIS_D70: U79.~AD31
- new net ARTEMIS_D71: U79.AD16
- new net ARTEMIS_D72: U79.AD34
- new net ARTEMIS_D73: J97.6, U86.~AD33/SWO
- new net ARTEMIS_D74: U86.~AD29
- new net ARTEMIS_D75: U86.~AD35
- new net ARTEMIS_D76: U86.~AD31
- new net ARTEMIS_D77: U86.AD16
- new net ARTEMIS_D78: U86.AD34
- new net ARTEMIS_D79: J105.6, U93.~AD33/SWO
- new net ARTEMIS_D80: U93.~AD29
- new net ARTEMIS_D81: U93.~AD35
- new net ARTEMIS_D82: U93.~AD31
- new net ARTEMIS_D83: U93.AD16
- new net ARTEMIS_D84: U93.AD34
- new net ARTEMIS_D85: J113.6, U100.~AD33/SWO
- new net ARTEMIS_D86: U100.~AD29
- new net ARTEMIS_D87: U100.~AD35
- new net ARTEMIS_D88: U100.~AD31
- new net ARTEMIS_D89: U100.AD16
- new net ARTEMIS_D90: U100.AD34
- new net ARTEMIS_D91: J121.6, U107.~AD33/SWO
- new net ARTEMIS_D92: U107.~AD29
- new net ARTEMIS_D93: U107.~AD35
- new net ARTEMIS_D94: U107.~AD31
- new net ARTEMIS_D95: U107.AD16
- new net ARTEMIS_D96: U107.AD34
- new net ARTEMIS_RX10: D73.C, U72.RXI-0, U73.8
- new net ARTEMIS_RX11: D80.C, U79.RXI-0, U80.8
- new net ARTEMIS_RX12: D87.C, U86.RXI-0, U87.8
- new net ARTEMIS_RX13: D94.C, U93.RXI-0, U94.8
- new net ARTEMIS_RX14: D101.C, U100.RXI-0, U101.8
- new net ARTEMIS_RX15: D108.C, U107.RXI-0, U108.8
- new net ARTEMIS_RX6: D45.C, U44.RXI-0, U45.8
- new net ARTEMIS_RX7: D52.C, U51.RXI-0, U52.8
- new net ARTEMIS_RX8: D59.C, U58.RXI-0, U59.8
- new net ARTEMIS_RX9: D66.C, U65.RXI-0, U66.8
- new net ARTEMIS_SWDCK10: J81.4, U72.SWDCK
- new net ARTEMIS_SWDCK11: J89.4, U79.SWDCK
- new net ARTEMIS_SWDCK12: J97.4, U86.SWDCK
- new net ARTEMIS_SWDCK13: J105.4, U93.SWDCK
- new net ARTEMIS_SWDCK14: J113.4, U100.SWDCK
- new net ARTEMIS_SWDCK15: J121.4, U107.SWDCK
- new net ARTEMIS_SWDCK6: J49.4, U44.SWDCK
- new net ARTEMIS_SWDCK7: J57.4, U51.SWDCK
- new net ARTEMIS_SWDCK8: J65.4, U58.SWDCK
- new net ARTEMIS_SWDCK9: J73.4, U65.SWDCK
- new net ARTEMIS_SWDIO10: J81.2, U72.SWDIO
- new net ARTEMIS_SWDIO11: J89.2, U79.SWDIO
- new net ARTEMIS_SWDIO12: J97.2, U86.SWDIO
- new net ARTEMIS_SWDIO13: J105.2, U93.SWDIO
- new net ARTEMIS_SWDIO14: J113.2, U100.SWDIO
- new net ARTEMIS_SWDIO15: J121.2, U107.SWDIO
- new net ARTEMIS_SWDIO6: J49.2, U44.SWDIO
- new net ARTEMIS_SWDIO7: J57.2, U51.SWDIO
- new net ARTEMIS_SWDIO8: J65.2, U58.SWDIO
- new net ARTEMIS_SWDIO9: J73.2, U65.SWDIO
- new net ARTEMIS_TX10: D74.C, U72.TXO-0, U73.9
- new net ARTEMIS_TX11: D81.C, U79.TXO-0, U80.9
- new net ARTEMIS_TX12: D88.C, U86.TXO-0, U87.9
- new net ARTEMIS_TX13: D95.C, U93.TXO-0, U94.9
- new net ARTEMIS_TX14: D102.C, U100.TXO-0, U101.9
- new net ARTEMIS_TX15: D109.C, U107.TXO-0, U108.9
- new net ARTEMIS_TX6: D46.C, U44.TXO-0, U45.9
- new net ARTEMIS_TX7: D53.C, U51.TXO-0, U52.9
- new net ARTEMIS_TX8: D60.C, U58.TXO-0, U59.9
- new net ARTEMIS_TX9: D67.C, U65.TXO-0, U66.9
- new net ARTEMIS_~AD12: J54.1, U44.~AD11
- new net ARTEMIS_~AD12/TX10: J78.3, U65.~AD12
- new net ARTEMIS_~AD12/TX11: J86.3, U72.~AD12
- new net ARTEMIS_~AD12/TX12: J94.3, U79.~AD12
- new net ARTEMIS_~AD12/TX13: J102.3, U86.~AD12
- new net ARTEMIS_~AD12/TX14: J110.3, U93.~AD12
- new net ARTEMIS_~AD12/TX15: J118.3, U100.~AD12
- new net ARTEMIS_~AD12/TX16: J126.3, U107.~AD12
- new net ARTEMIS_~AD12/TX7: J54.3, U44.~AD12
- new net ARTEMIS_~AD12/TX8: J62.3, U51.~AD12
- new net ARTEMIS_~AD12/TX9: J70.3, U58.~AD12
- new net ARTEMIS_~AD13: J54.4, U44.~AD32
- new net ARTEMIS_~AD13/RX10: J78.2, U65.~AD13
- new net ARTEMIS_~AD13/RX11: J86.2, U72.~AD13
- new net ARTEMIS_~AD13/RX12: J94.2, U79.~AD13
- new net ARTEMIS_~AD13/RX13: J102.2, U86.~AD13
- new net ARTEMIS_~AD13/RX14: J110.2, U93.~AD13
- new net ARTEMIS_~AD13/RX15: J118.2, U100.~AD13
- new net ARTEMIS_~AD13/RX16: J126.2, U107.~AD13
- new net ARTEMIS_~AD13/RX7: J54.2, U44.~AD13
- new net ARTEMIS_~AD13/RX8: J62.2, U51.~AD13
- new net ARTEMIS_~AD13/RX9: J70.2, U58.~AD13
- new net ARTEMIS_~AD14: J62.1, U51.~AD11
- new net ARTEMIS_~AD15: J62.4, U51.~AD32
- new net ARTEMIS_~AD16: J70.1, U58.~AD11
- new net ARTEMIS_~AD17: J70.4, U58.~AD32
- new net ARTEMIS_~AD18: J78.1, U65.~AD11
- new net ARTEMIS_~AD19: J78.4, U65.~AD32
- new net ARTEMIS_~AD20: J86.1, U72.~AD11
- new net ARTEMIS_~AD21: J86.4, U72.~AD32
- new net ARTEMIS_~AD22: J94.1, U79.~AD11
- new net ARTEMIS_~AD23: J94.4, U79.~AD32
- new net ARTEMIS_~AD24: J102.1, U86.~AD11
- new net ARTEMIS_~AD25: J102.4, U86.~AD32
- new net ARTEMIS_~AD26: J110.1, U93.~AD11
- new net ARTEMIS_~AD27: J110.4, U93.~AD32
- new net ARTEMIS_~AD28: J118.1, U100.~AD11
- new net ARTEMIS_~AD29: J118.4, U100.~AD32
- new net ARTEMIS_~AD30: J126.1, U107.~AD11
- new net ARTEMIS_~AD31: J126.4, U107.~AD32
- new net CC13: J55.B5, R127.2
- new net CC14: J55.A5, R128.2
- new net CC15: J63.B5, R147.2
- new net CC16: J63.A5, R148.2
- new net CC17: J71.B5, R167.2
- new net CC18: J71.A5, R168.2
- new net CC19: J79.B5, R187.2
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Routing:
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- added copper zone on layer 1, net GND10
- added copper zone on layer 16, net GND10
- added copper zone on layer 1, net GND11
- added copper zone on layer 16, net GND11
- added copper zone on layer 1, net GND12
- added copper zone on layer 16, net GND12
- added copper zone on layer 1, net GND13
- added copper zone on layer 16, net GND13
- added copper zone on layer 1, net GND14
- added copper zone on layer 16, net GND14
- added copper zone on layer 1, net GND15
- added copper zone on layer 16, net GND15
- added copper zone on layer 1, net GND6
- added copper zone on layer 16, net GND6
- added copper zone on layer 1, net GND7
- added copper zone on layer 16, net GND7
- added copper zone on layer 1, net GND8
- added copper zone on layer 16, net GND8
- added copper zone on layer 1, net GND9
- added copper zone on layer 16, net GND9
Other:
- board size 106.2 x 95.2 mm -> 137.2 x 167 mm
- board text added: "x04"
- board text removed: "x03"
